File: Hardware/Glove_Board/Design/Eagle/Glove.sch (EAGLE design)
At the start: 1 part

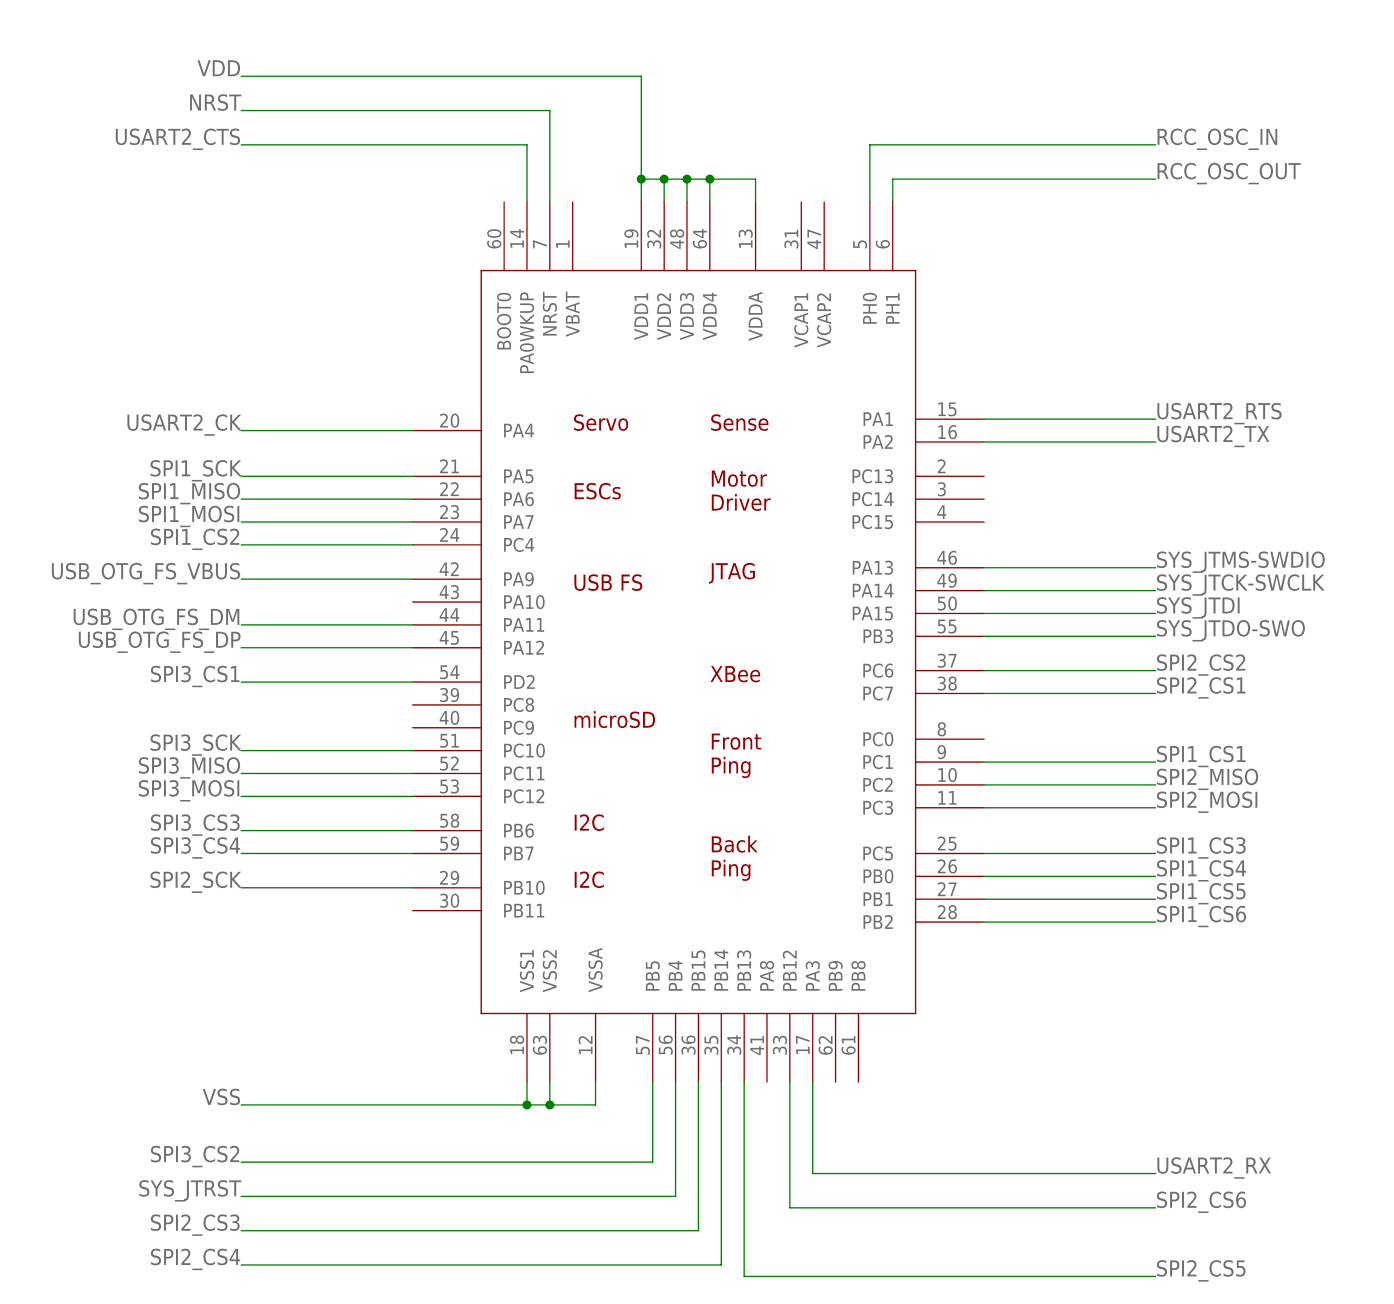
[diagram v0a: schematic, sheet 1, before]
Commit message: Added Power and Oscillator to schematic
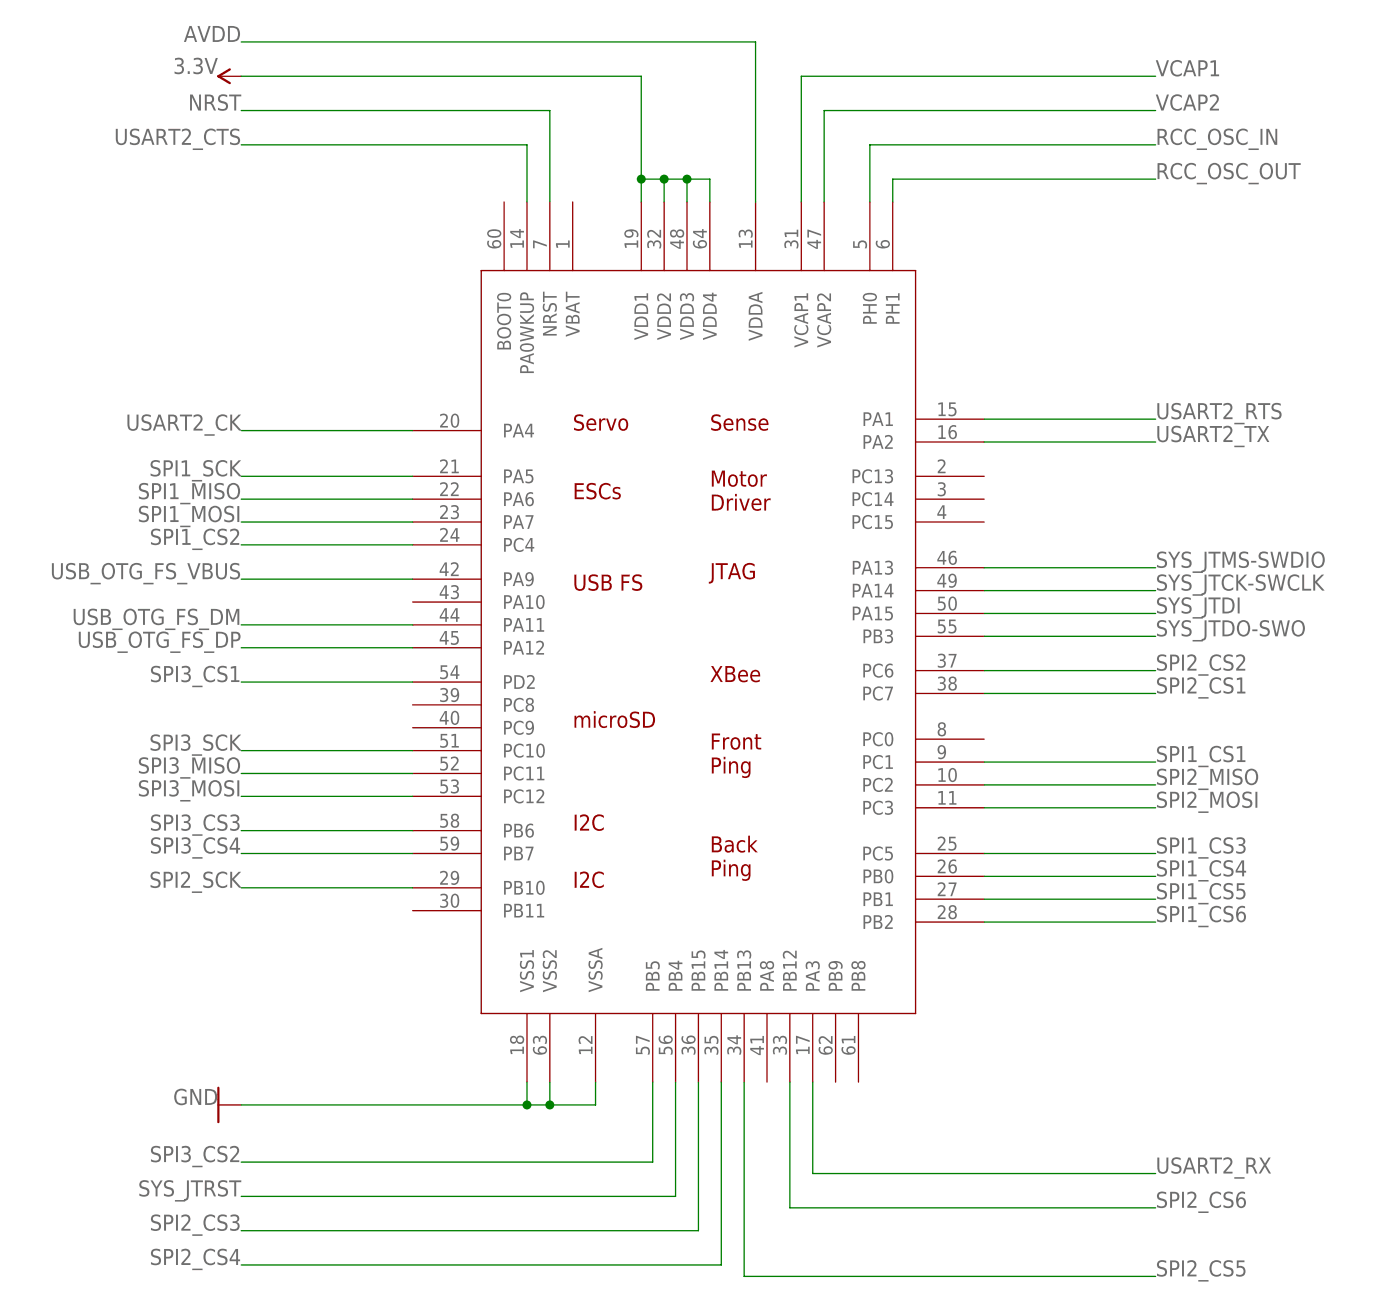
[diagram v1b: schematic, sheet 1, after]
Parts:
- added C1, C4, C5, C6, C7, C8: 100nF, rcl:C-USC0805K
- added C10, C9: 2.2uF, rcl:C-USC0805K
- added C11, C13: 0.1uF, rcl:C-USC0805K
- added C12, C14: 10uF, rcl:CPOL-USSMCD
- added C2, C3: 25pF, rcl:C-USC0805K
- added D1: RED, SparkFun-LED:LED-RED1206
- added FB1: 30Ω/1.8A, SparkFun-Coils:FERRITE_BEAD-0603
- added IC1: LM1117MPX-3.3, lm1117:LM1117MPX-3.3
- added J1: (no value), SparkFun-Connectors:USB_MICRO-BREDUCED_PASTE
- added J2: CORTEX_DEBUG_PTH, SparkFun-Connectors:CORTEX_DEBUG_PTH
- added J4: (no value), SparkFun-Connectors:CONN_06SILK_FEMALE_PTH
- added Q1: 8MHz, SparkFun-Clocks:CRYSTAL-8MHZSMD-5X3.2
- added R1, R2: 0, rcl:R-US_R0805
- added R3: 100, rcl:R-US_R0805
- added R4: 100K, rcl:R-US_R0805
- added R5: 1k, rcl:R-US_R0805
- added S2: (no value), switch-omron:10-XX
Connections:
- removed net VDD: U$1.VDD1, U$1.VDD2, U$1.VDD3, U$1.VDD4, U$1.VDDA
- removed net VSS: U$1.VSS1, U$1.VSS2, U$1.VSSA
- new net +5V: C11.1, C14.+, IC1.IN, R5.1
- new net 3.3V: C12.+, C13.1, C4.1, C5.1, C6.1, C7.1, FB1.2, IC1.OUT, IC1.OUT1, U$1.VDD1, U$1.VDD2, U$1.VDD3, U$1.VDD4
- new net 5V: J1.VBUS
- new net AVDD: C8.1, FB1.1, U$1.VDDA
- new net GND: C10.2, C11.2, C12.-, C13.2, C14.-, C2.2, C3.2, C4.2, C5.2, C6.2, C7.2, C8.2, C9.2, D1.C, IC1.GND, J1.GND, J1.SHIELD, R3.2, R4.2, S2.S, S2.S1, U$1.VSS1, U$1.VSS2, U$1.VSSA
- new net N$1: C1.2, R3.1
- new net N$2: C2.1, Q1.1, R1.1
- new net N$3: C3.1, Q1.2, R2.1
- new net N$4: J2.!RESET
- new net N$5: J1.ID, R4.1
- new net N$6: D1.A, R5.2
- new net VCAP1: C9.1, U$1.VCAP1
- new net VCAP2: C10.1, U$1.VCAP2
- net NRST: now also C1.1, S2.P, S2.P1
- net RCC_OSC_IN: now also R1.2
- net RCC_OSC_OUT: now also R2.2
- net USB_OTG_FS_DM: now also J1.D-
- net USB_OTG_FS_DP: now also J1.D+
